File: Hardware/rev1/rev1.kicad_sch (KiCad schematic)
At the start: 15 parts, among them J1 USB_C_Receptacle_USB2.0_14P, U1 STM32F103C8Tx, U2 HT75xx-1-SOT89

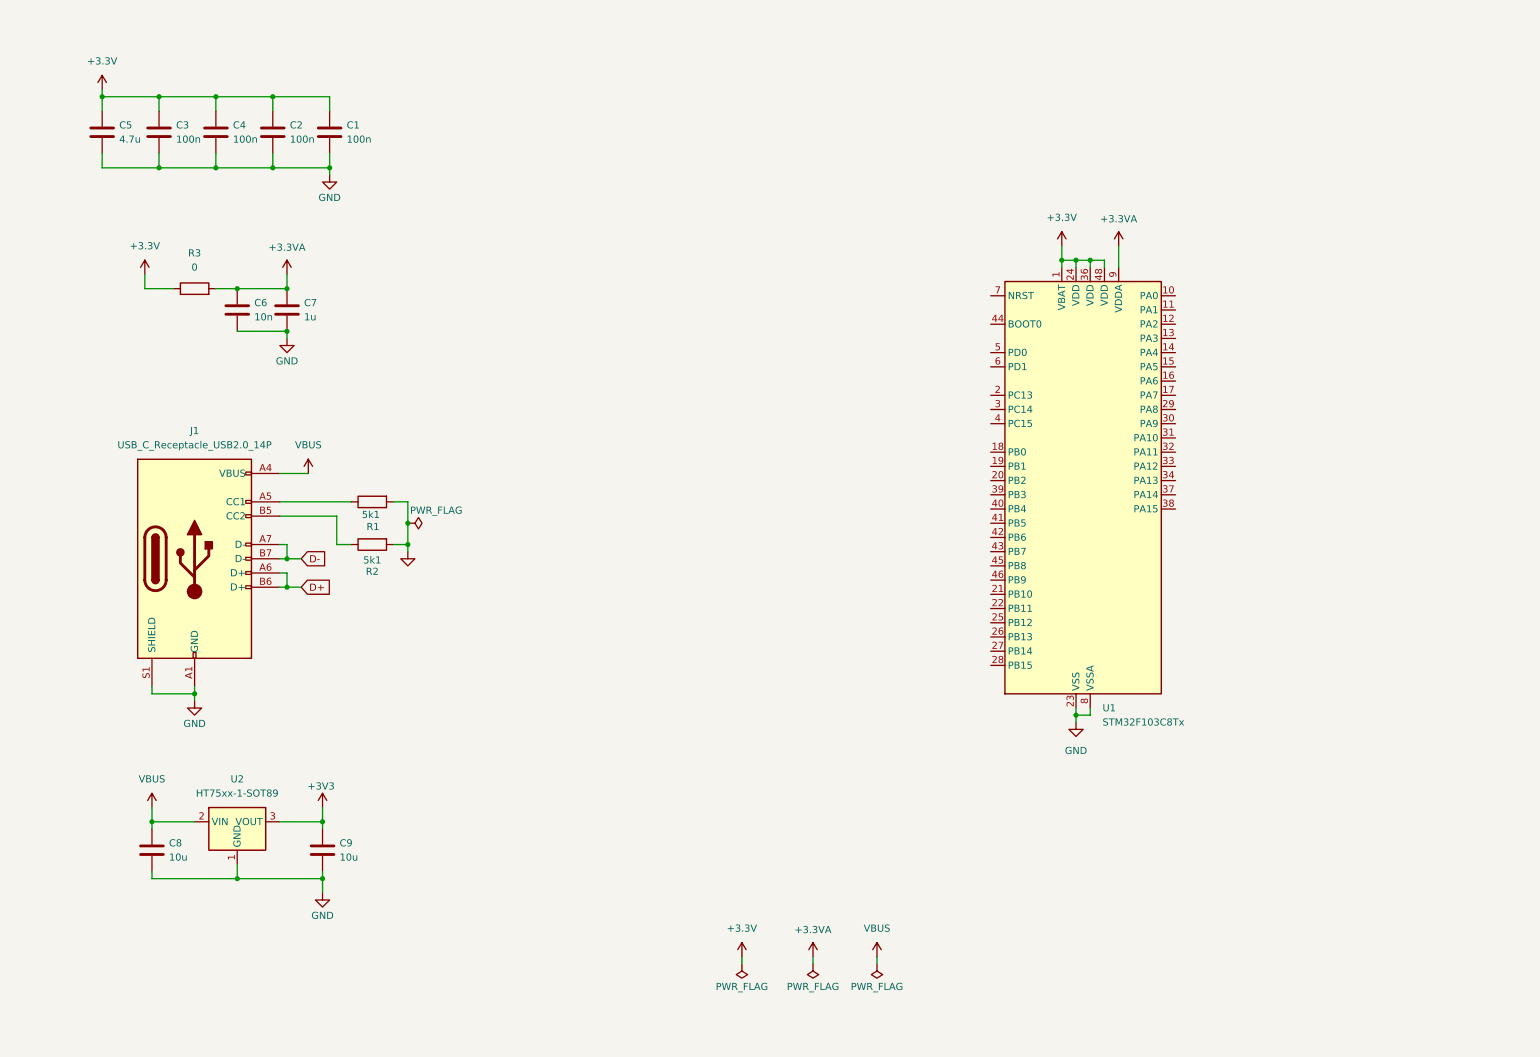
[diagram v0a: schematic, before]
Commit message: Pressure sensor and debugging added
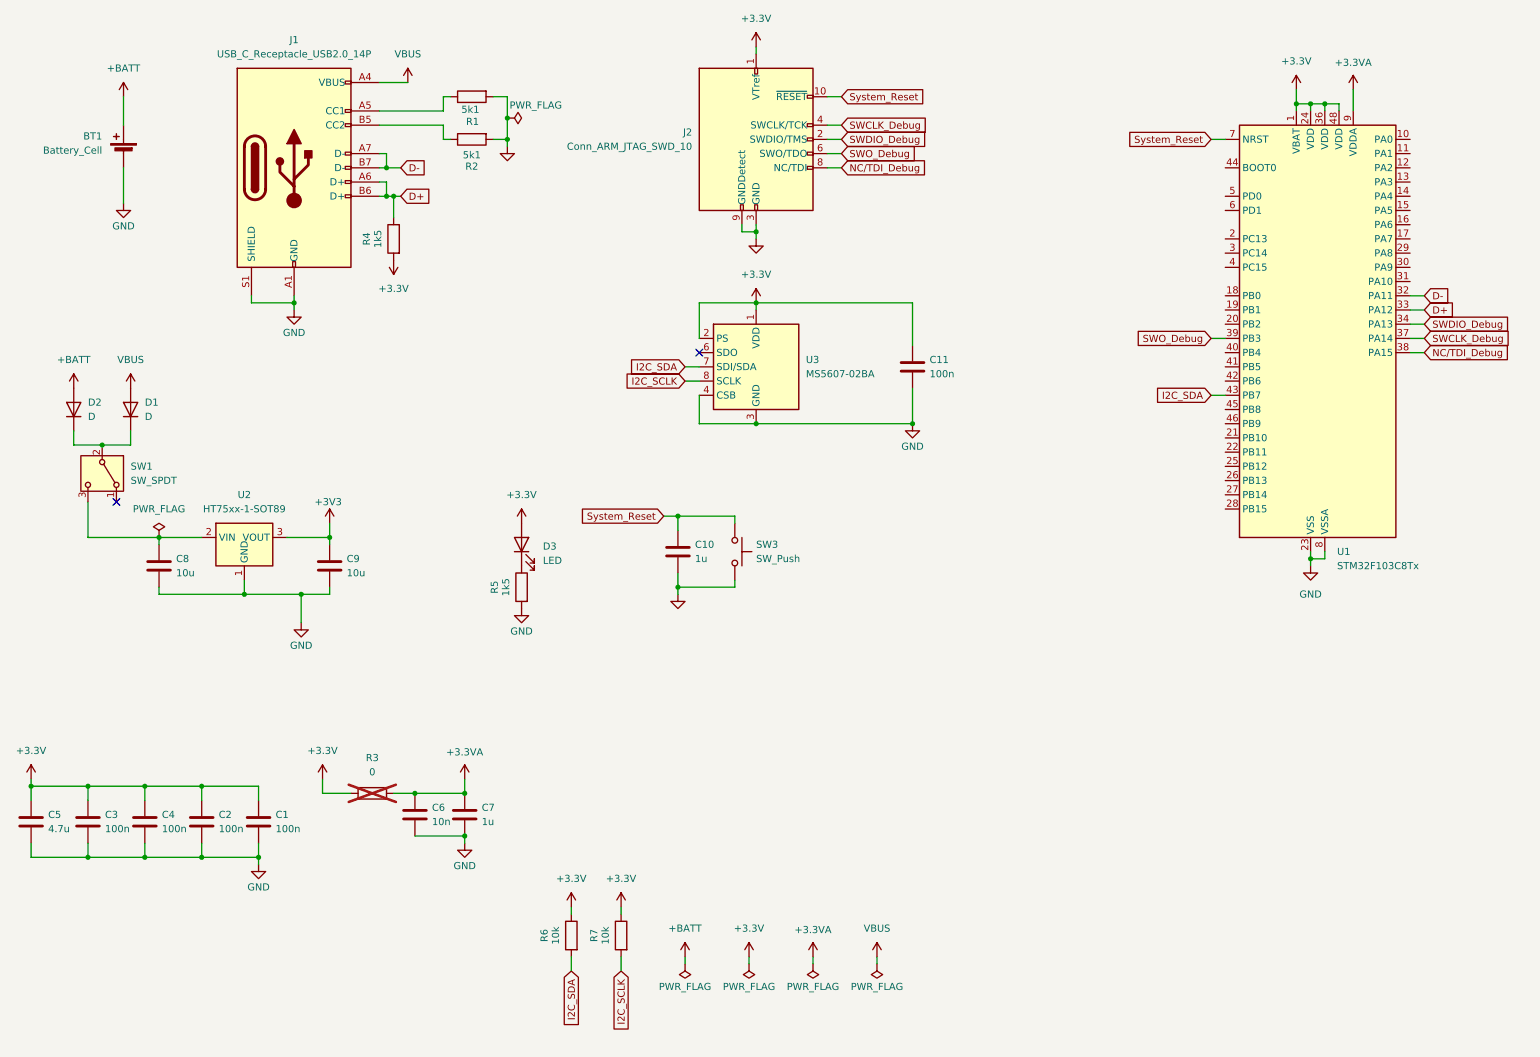
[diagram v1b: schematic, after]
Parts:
- added BT1: Battery_Cell, symbol Device:Battery_Cell
- added C10: 1u, symbol Device:C
- added C11: 100n, symbol Device:C
- added D1, D2: D, symbol Device:D
- added D3: LED, symbol Device:LED
- added J2: Conn_ARM_JTAG_SWD_10, symbol Connector:Conn_ARM_JTAG_SWD_10
- added R4, R5: 1k5, Resistor_SMD:R_0402_1005Metric, symbol Device:R
- added R6, R7: 10k, Resistor_SMD:R_0402_1005Metric, symbol Device:R
- added SW1: SW_SPDT, symbol Switch:SW_SPDT
- added SW3: SW_Push, symbol Switch:SW_Push
- added U3: MS5607-02BA, Package_LGA:LGA-8_3x5mm_P1.25mm, symbol Sensor_Pressure:MS5607-02BA
- R3: now not fitted
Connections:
- net +3.3V: now also C11.1, D3.2 (A), J2.1 (VTref), R4.2, R6.1, R7.1, U3.1 (VDD), U3.2 (PS)
- net D+: now also U1.33 (PA12), R4.1
- net D-: now also U1.32 (PA11)
- net GND: now also BT1.2 (-), C10.2, C11.2, J2.3 (GND), J2.5 (GND), J2.9 (GNDDetect), R5.2, SW3.2, U3.3 (GND), U3.4 (CSB), U3.5 (CSB)
- net VBUS: now also D1.2 (A); no longer C8.1, U2.2 (VIN)
- net SWDIO_Debug: now reaches U1.34 (PA13)
- net SWDIO_Debug: now also J2.2 (SWDIO/TMS)
- net SWCLK_Debug: now reaches U1.37 (PA14)
- net SWCLK_Debug: now also J2.4 (SWCLK/TCK)
- net NC/TDI_Debug: now reaches U1.38 (PA15)
- net NC/TDI_Debug: now also J2.8 (NC/TDI)
- net SWO_Debug: now reaches U1.39 (PB3)
- net SWO_Debug: now also J2.6 (SWO/TDO)
- net I2C_SDA: now reaches U1.43 (PB7)
- net I2C_SDA: now also R6.2, U3.7 (SDI/SDA)
- net System_Reset: now reaches U1.7 (NRST)
- net System_Reset: now also C10.1, J2.10 (~{RESET}), SW3.1
- new net: C8.1, SW1.3 (C), U2.2 (VIN)
- new net: D1.1 (K), D2.1 (K), SW1.2 (B)
- new net: D3.1 (K), R5.1
- new net +BATT: BT1.1 (+), D2.2 (A)
- new net I2C_SCLK: R7.2, U3.8 (SCLK)
- no-connect marks 0 -> 2
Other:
- moved on the sheet: C1, C2, C3, C4, C5, C6, C7, C8, C9, J1, R1, R2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

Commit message: Added Flash, Buzzer
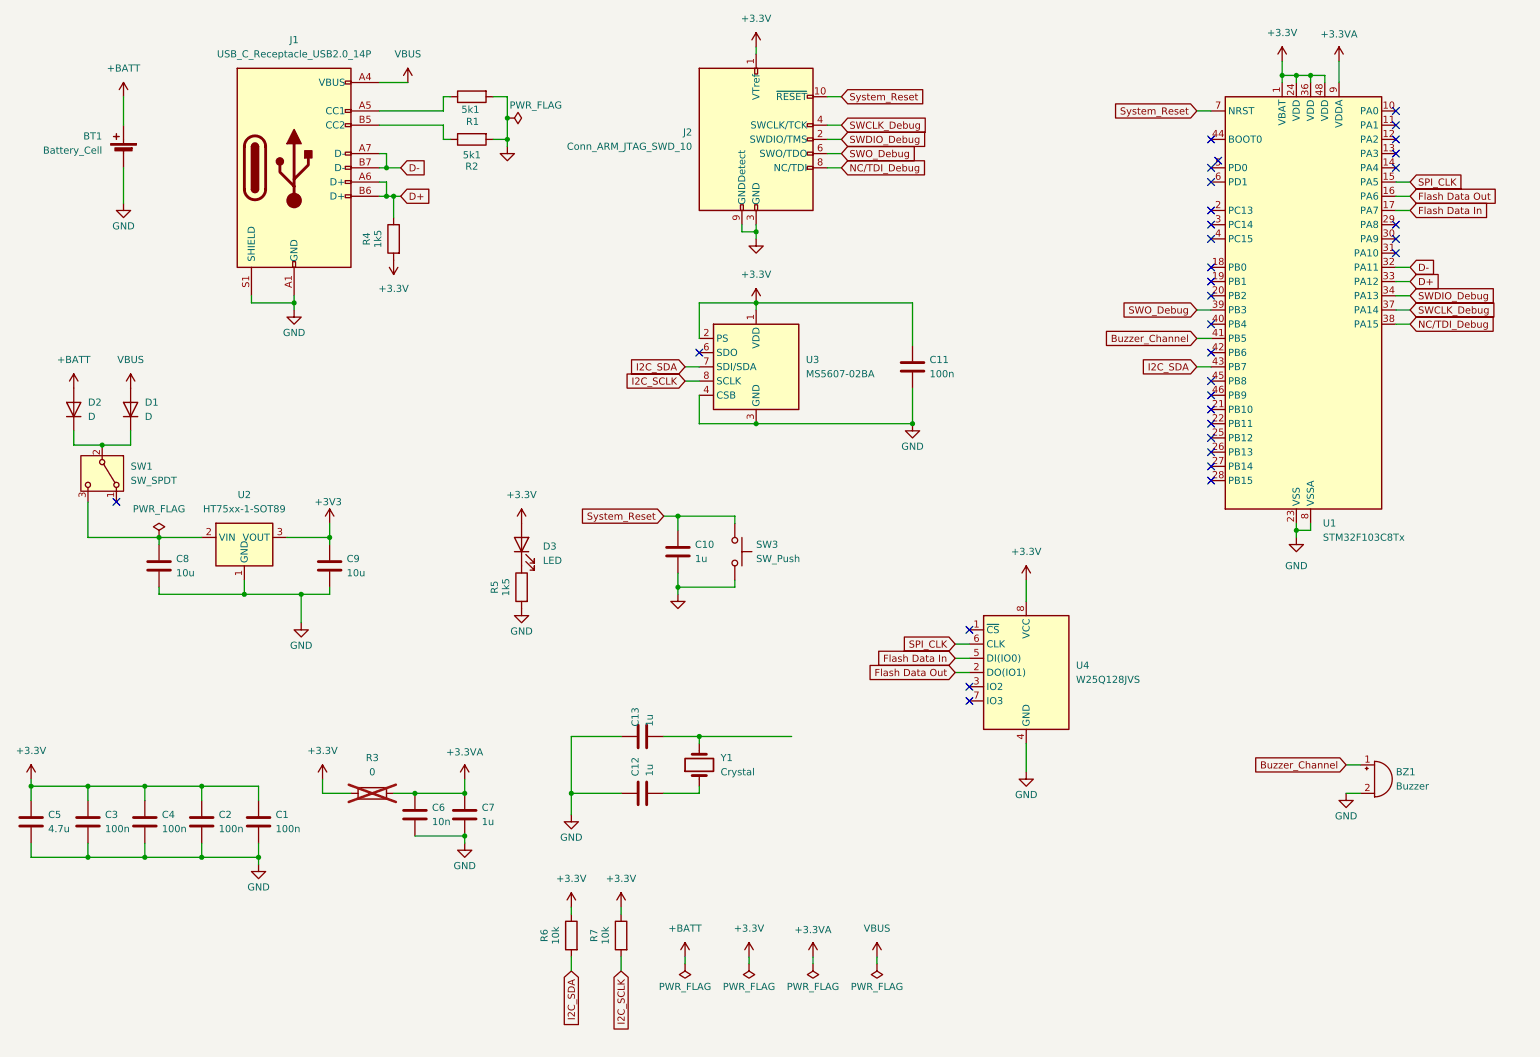
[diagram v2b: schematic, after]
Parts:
- added BZ1: Buzzer, symbol Device:Buzzer
- added C12, C13: 1u, symbol Device:C
- added U4: W25Q128JVS, Package_SO:SOIC-8_5.23x5.23mm_P1.27mm, symbol Memory_Flash:W25Q128JVS
- added Y1: Crystal, symbol Device:Crystal
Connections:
- net +3.3V: now also U4.8 (VCC)
- net GND: now also BZ1.2 (-), C12.1, C13.1, U4.4 (GND)
- net SPI_CLK: now reaches U1.15 (PA5)
- net SPI_CLK: now also U4.6 (CLK)
- net Flash Data Out: now reaches U1.16 (PA6)
- net Flash Data Out: now also U4.2 (DO(IO1))
- net Flash Data In: now reaches U1.17 (PA7)
- net Flash Data In: now also U4.5 (DI(IO0))
- net Buzzer_Channel: now reaches U1.41 (PB5)
- net Buzzer_Channel: now also BZ1.1 (+)
- new net: C12.2, Y1.1
- new net: C13.2, Y1.2
- no-connect marks 2 -> 33
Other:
- company: (none) -> StrathGREM Ltd.
- title: (none) -> Gremlinising
- moved on the sheet: U1

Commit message: Some cleanup
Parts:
- removed C12, C13: 1u, symbol Device:C
- removed Y1: Crystal, symbol Device:Crystal
- added C14, C15: 10p, Capacitor_SMD:C_0402_1005Metric, symbol Device:C
- added Y2: 16MHz, Crystal:Crystal_SMD_3225-4Pin_3.2x2.5mm, symbol Device:Crystal_GND23_Small
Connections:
- net I2C_SCLK is gone; now on net I2C2_SCK: R7.2, U3.8 (SCLK)
- net GND: now also C14.2, C15.2, Y2.2, Y2.3
- net I2C2_SCK: now reaches U1.42 (PB6)
- net HSE_IN: now reaches U1.5 (PD0)
- net HSE_IN: now also C14.1, Y2.1
- net HSE_OUT: now reaches U1.6 (PD1)
- net HSE_OUT: now also C15.1, Y2.4
- net I2C_SDA renamed I2C2_SDA
- no-connect marks 33 -> 29
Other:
- note added: "CL=2*(CLO-Cs) = 2*(10-5) = 10pF"
- moved on the sheet: BZ1, C10, C11, D3, R1, R2, R4, R5, R6, R7, SW3, U3

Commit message: Did some stuff aye
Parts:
- removed BT1: Battery_Cell, symbol Device:Battery_Cell
- removed BZ1: Buzzer, symbol Device:Buzzer
- removed C1, C11, C2, C3, C4: 100n, symbol Device:C
- removed C10, C7: 1u, symbol Device:C
- removed C14, C15: 10p, Capacitor_SMD:C_0402_1005Metric, symbol Device:C
- removed C5: 4.7u, symbol Device:C
- removed C6: 10n, symbol Device:C
- removed C8, C9: 10u, symbol Device:C
- removed D1, D2: D, symbol Device:D
- removed D3: LED, symbol Device:LED
- removed J1: USB_C_Receptacle_USB2.0_14P, symbol Connector:USB_C_Receptacle_USB2.0_14P
- removed J2: Conn_ARM_JTAG_SWD_10, symbol Connector:Conn_ARM_JTAG_SWD_10
- removed R1, R2: 5k1, Resistor_SMD:R_0402_1005Metric, symbol Device:R
- removed R3: 0, symbol Device:R
- removed R4, R5: 1k5, Resistor_SMD:R_0402_1005Metric, symbol Device:R
- removed R6, R7: 10k, Resistor_SMD:R_0402_1005Metric, symbol Device:R
- removed SW1: SW_SPDT, symbol Switch:SW_SPDT
- removed SW3: SW_Push, symbol Switch:SW_Push
- removed U1: STM32F103C8Tx, Package_QFP:LQFP-48_7x7mm_P0.5mm, symbol MCU_ST_STM32F1:STM32F103C8Tx
- removed U2: HT75xx-1-SOT89, Package_TO_SOT_SMD:SOT-89-3, symbol Regulator_Linear:HT75xx-1-SOT89
- removed U3: MS5607-02BA, Package_LGA:LGA-8_3x5mm_P1.25mm, symbol Sensor_Pressure:MS5607-02BA
- removed U4: W25Q128JVS, Package_SO:SOIC-8_5.23x5.23mm_P1.27mm, symbol Memory_Flash:W25Q128JVS
- removed Y2: 16MHz, Crystal:Crystal_SMD_3225-4Pin_3.2x2.5mm, symbol Device:Crystal_GND23_Small
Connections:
- no-connect marks 29 -> 0
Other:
- added sheet Interface and Debugging (Interface_and_debugging.kicad_sch)
- added sheet MCU et al Sheet (MCU.kicad_sch)
- added sheet Power Sheet (untitled.kicad_sch)
- added sheet Pressure Sensor (Pressure_Sensor.kicad_sch)
- note removed: "CL=2*(CLO-Cs) = 2*(10-5) = 10pF"

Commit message: h
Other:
- removed sheet Interface and Debugging
- removed sheet MCU et al Sheet
- removed sheet Pressure Sensor
- added sheet Microcontroller (mcu.kicad_sch)
- sheet Power Sheet ports: added USB; removed none
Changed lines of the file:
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@@
 		(company "StrathGREM Ltd.")
 	)
+	(wire
+		(pts
+			(xy 144.78 95.25) (xy 152.4 95.25)
+		)
+		(stroke
+			(width 0)
+			(type default)
+		)
+	)
 	(sheet
-		(at 36.83 102.87)
+		(at 152.4 77.47)
 		(size 58.42 36.83)
 		(fields_autoplaced yes)
@@
 			(color 0 0 0 0.0000)
 		)
-		(property "Sheetname" "Pressure Sensor"
-			(at 36.83 102.1584 0)
+		(property "Sheetname" "Microcontroller"
+			(at 152.4 76.7584 0)
 			(effects
 				(font
@@
 			)
 		)
-		(property "Sheetfile" "Pressure_Sensor.kicad_sch"
-			(at 36.83 140.2846 0)
+		(property "Sheetfile" "mcu.kicad_sch"
+			(at 152.4 114.8846 0)
 			(effects
 				(font
@@
 				)
 				(justify left top)
+			)
+		)
+		(pin "USB" bidirectional
+			(at 152.4 95.25 180)
+			(effects
+				(font
+					(size 1.27 1.27)
+				)
+				(justify left)
 			)
 		)
@@
 	)
 	(sheet
-		(at 36.83 35.56)
+		(at 86.36 77.47)
 		(size 58.42 36.83)
 		(fields_autoplaced yes)
@@
 		)
 		(property "Sheetname" "Power Sheet"
-			(at 36.83 34.8484 0)
+			(at 86.36 76.7584 0)
 			(effects
 				(font
@@
 		)
 		(property "Sheetfile" "untitled.kicad_sch"
-			(at 36.83 72.9746 0)
+			(at 86.36 114.8846 0)
 			(effects
 				(font
@@
 				)
 				(justify left top)
+			)
+		)
+		(pin "USB" bidirectional
+			(at 144.78 95.25 0)
+			(effects
+				(font
+					(size 1.27 1.27)
+				)
+				(justify right)
 			)
 		)
@@
 				)
 			)
-		)
-	)
-	(sheet
-		(at 163.83 102.87)
-		(size 58.42 36.83)
-		(fields_autoplaced yes)
-		(stroke
-			(width 0.1524)
-			(type solid)
-		)
-		(fill
-			(color 0 0 0 0.0000)
-		)
-		(property "Sheetname" "Interface and Debugging"
-			(at 163.83 102.1584 0)
-			(effects
-				(font
-					(size 1.27 1.27)
-				)
-				(justify left bottom)
-			)
-		)
-		(property "Sheetfile" "Interface_and_debugging.kicad_sch"
-			(at 163.83 140.2846 0)
-			(effects
-				(font
-					(size 1.27 1.27)
-				)
-				(justify left top)
-			)
-		)
-		(instances
-			(project "rev1"
-				(path "/e52639ab-1647-4d34-8bc5-5aadc4708147"
-					(page "4")
-				)
-			)
-		)
-	)
-	(sheet
-		(at 163.83 35.56)
-		(size 58.42 36.83)
-		(fields_autoplaced yes)
-		(stroke
-			(width 0.1524)
-			(type solid)
-		)
-		(fill
-			(color 0 0 0 0.0000)
-		)
-		(property "Sheetname" "MCU et al Sheet"
-			(at 163.83 34.8484 0)
-			(effects
-				(font
-					(size 1.27 1.27)
-				)
-				(justify left bottom)
-			)
-		)
-		(property "Sheetfile" "MCU.kicad_sch"
-			(at 163.83 72.9746 0)
-			(effects
-				(font
-					(size 1.27 1.27)
-				)
-				(justify left top)
-			)
-		)
-		(instances
-			(project "rev1"
-				(path "/e52639ab-1647-4d34-8bc5-5aadc4708147"
-					(page "3")
-				)
-			)

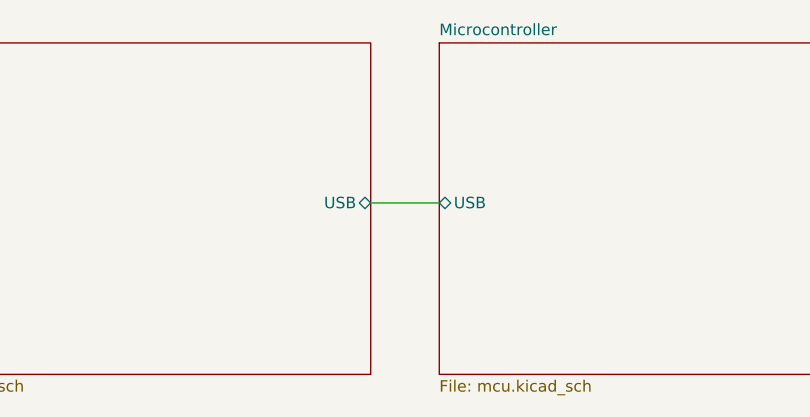
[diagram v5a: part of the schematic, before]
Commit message: Fixed the Errors
The Nets i tells ya, the nets!
need to specify the signals in the hierarchal labels
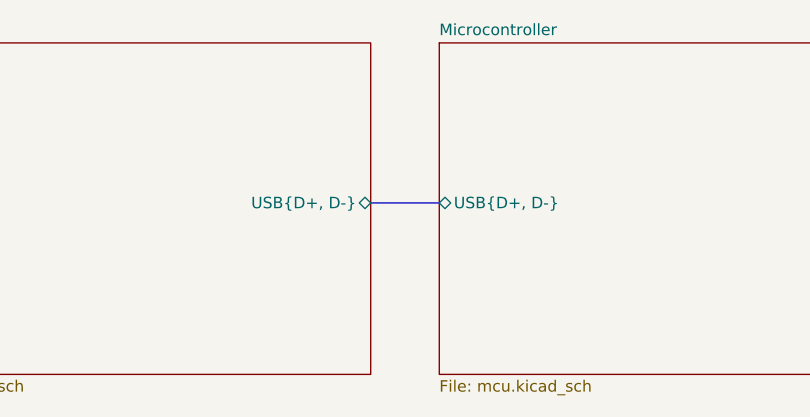
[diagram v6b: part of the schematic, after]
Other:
- sheet Microcontroller ports: added USB{D+, D-}; removed USB
- sheet Power Sheet ports: added USB{D+, D-}; removed USB
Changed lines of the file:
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@@
 		(company "StrathGREM Ltd.")
 	)
-	(wire
+	(bus
 		(pts
 			(xy 144.78 95.25) (xy 152.4 95.25)
@@
 			)
 		)
-		(pin "USB" bidirectional
+		(pin "USB{D+, D-}" bidirectional
 			(at 152.4 95.25 180)
 			(effects
@@
 			)
 		)
-		(pin "USB" bidirectional
+		(pin "USB{D+, D-}" bidirectional
 			(at 144.78 95.25 0)
 			(effects

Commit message: Add buses (maybe)
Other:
- sheet Power Sheet renamed Power
- added sheet Peripherals (Pressure_Sensor.kicad_sch)
- sheet Microcontroller ports: added DEBUG{TMS/SWDIO, JTCK/SWCLK, JTDI/NC, JTDO/SWO}, I2C2{SCK, SDA}, SPI1{SCLK, MISO, MOSI}; removed none
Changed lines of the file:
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@@
 	(bus
 		(pts
-			(xy 144.78 95.25) (xy 152.4 95.25)
+			(xy 143.51 57.15) (xy 151.13 57.15)
 		)
 		(stroke
@@
 	)
 	(sheet
-		(at 152.4 77.47)
+		(at 151.13 39.37)
 		(size 58.42 36.83)
 		(fields_autoplaced yes)
@@
 		)
 		(property "Sheetname" "Microcontroller"
-			(at 152.4 76.7584 0)
+			(at 151.13 38.6584 0)
 			(effects
 				(font
@@
 		)
 		(property "Sheetfile" "mcu.kicad_sch"
-			(at 152.4 114.8846 0)
+			(at 151.13 76.7846 0)
 			(effects
 				(font
@@
 		)
 		(pin "USB{D+, D-}" bidirectional
-			(at 152.4 95.25 180)
+			(at 151.13 57.15 180)
 			(effects
 				(font
@@
 			)
 		)
+		(pin "DEBUG{TMS{slash}SWDIO, JTCK{slash}SWCLK, JTDI{slash}NC, JTDO{slash}SWO}"
+			bidirectional
+			(at 209.55 43.18 0
+			)
+			(effects
+				(font
+					(size 1.27 1.27)
+				)
+				(justify right)
+			)
+		)
+		(pin "SPI1{SCLK, MISO, MOSI}" bidirectional
+			(at 209.55 45.72 0)
+			(effects
+				(font
+					(size 1.27 1.27)
+				)
+				(justify right)
+			)
+		)
+		(pin "I2C2{SCK, SDA}" bidirectional
+			(at 209.55 48.26 0)
+			(effects
+				(font
+					(size 1.27 1.27)
+				)
+				(justify right)
+			)
+		)
 		(instances
 			(project "rev1"
 				(path "/e52639ab-1647-4d34-8bc5-5aadc4708147"
-					(page "5")
+					(page "3")
 				)
 			)
@@
 	)
 	(sheet
-		(at 86.36 77.47)
+		(at 85.09 39.37)
 		(size 58.42 36.83)
 		(fields_autoplaced yes)
@@
 			(color 0 0 0 0.0000)
 		)
-		(property "Sheetname" "Power Sheet"
-			(at 86.36 76.7584 0)
+		(property "Sheetname" "Power"
+			(at 85.09 38.6584 0)
 			(effects
 				(font
@@
 		)
 		(property "Sheetfile" "untitled.kicad_sch"
-			(at 86.36 114.8846 0)
+			(at 85.09 76.7846 0)
 			(effects
 				(font
@@
 		)
 		(pin "USB{D+, D-}" bidirectional
-			(at 144.78 95.25 0)
+			(at 143.51 57.15 0)
 			(effects
 				(font
@@
 				)
 			)
+		)
+	)
+	(sheet
+		(at 146.05 96.52)
+		(size 68.58 25.4)
+		(fields_autoplaced yes)
+		(stroke
+			(width 0.1524)
+			(type solid)
+		)
+		(fill
+			(color 0 0 0 0.0000)
+		)
+		(property "Sheetname" "Peripherals"
+			(at 146.05 95.8084 0)
+			(effects
+				(font
+					(size 1.27 1.27)
+				)
+				(justify left bottom)
+			)
+		)
+		(property "Sheetfile" "Pressure_Sensor.kicad_sch"
+			(at 146.05 122.5046 0)
+			(effects
+				(font
+					(size 1.27 1.27)
+				)
+				(justify left top)
+			)
+		)
+		(property "Field2" ""
+			(at 146.05 96.52 0)
+			(effects
+				(font
+					(size 1.27 1.27)
+				)
+				(hide yes)
+			)
+		)
+		(instances
+			(project "rev1"
+				(path "/e52639ab-1647-4d34-8bc5-5aadc4708147"
+					(page "4")
+				)
+			)
